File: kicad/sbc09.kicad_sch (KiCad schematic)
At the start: 77 parts, among them J1 Conn_01x03_Male, J2 Conn_01x06_Male, J3 Conn_01x06_Male, J4 Conn_01x06_Male, J5 DB9_Female_MountingHoles, J6 Conn_02x25_Odd_Even, Q1 2N7000, SW1 SW_Push, U1 74LS245, U10 74LS670, U11 74LS670, U12 AS6C4008-55PCN, U13 SST39SF040-DIP, U14 SST39SF040-DIP, U15 XR68C681CJ, U16 MAX232, U2 74LS245, U3 74LS245, U4 MC6809E, U5 74HCT125, U6 ATF22V10C, U7 ATF22V10C, U8 74LS670, U9 74LS670, X1 8MHz, X2 3.6864MHz

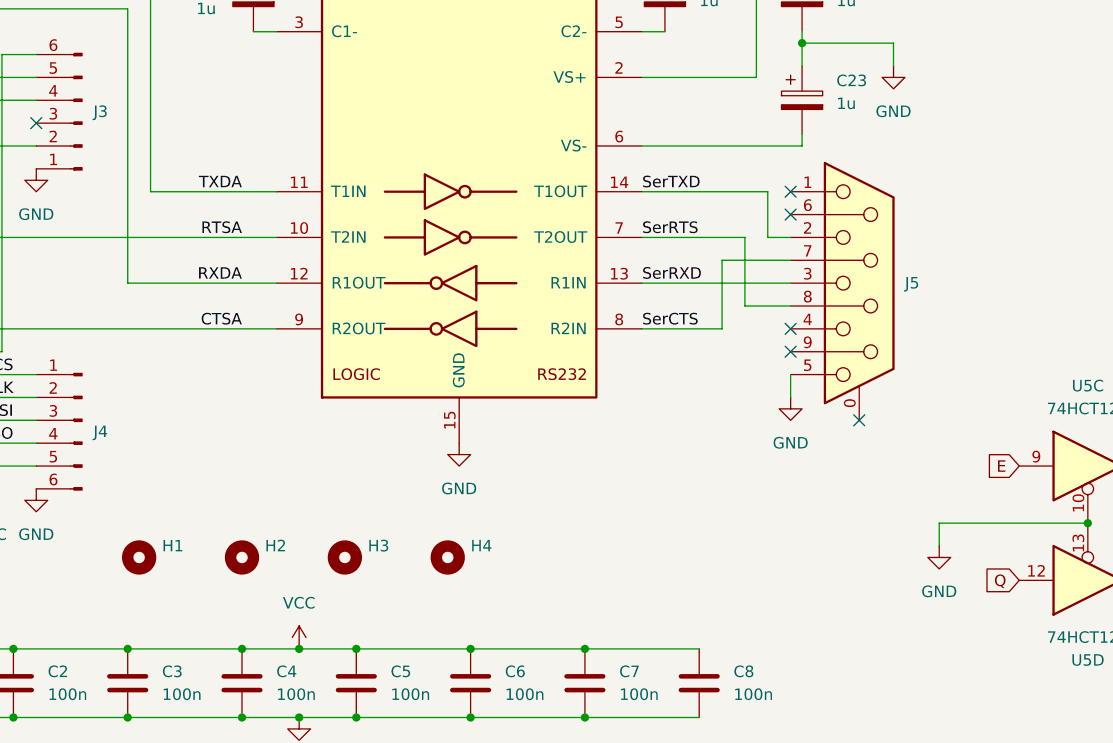
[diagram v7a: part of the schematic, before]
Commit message: Replaced 9-pin D-Sub with 10-pin header
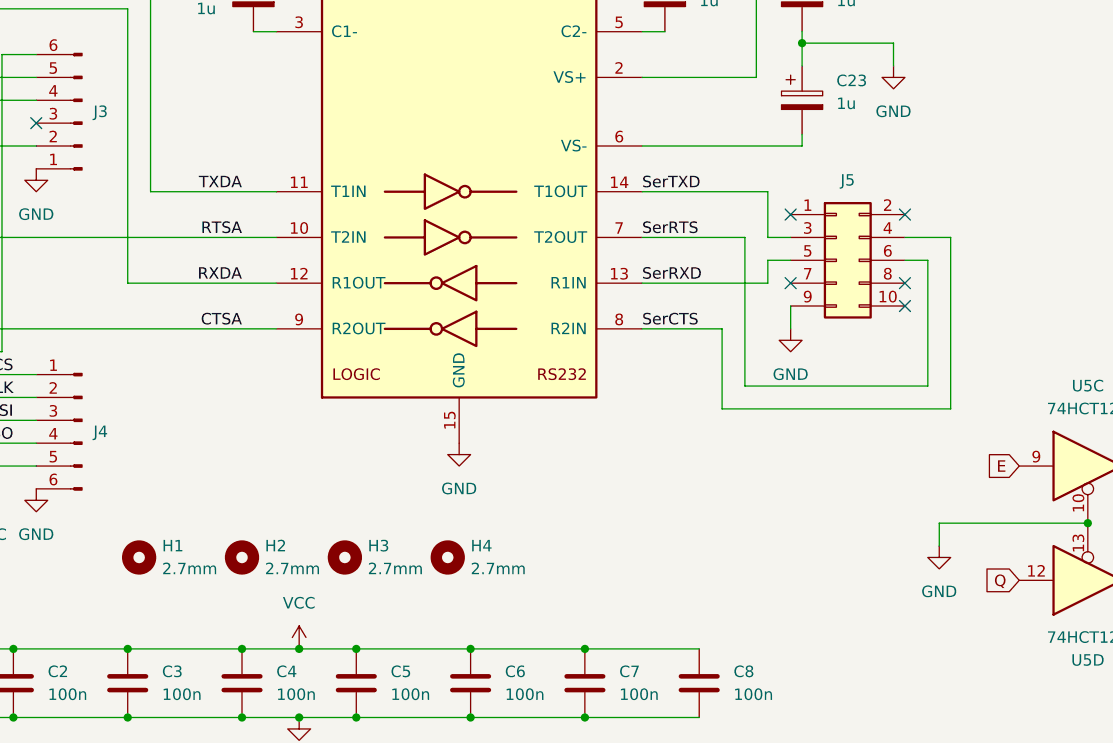
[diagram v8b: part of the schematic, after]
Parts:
- removed J5: DB9_Female_MountingHoles, Connector_Dsub:DSUB-9_Female_Horizontal_P2.77x2.84mm_EdgePinOffset7.70mm_Housed_MountingHolesOffset9.12mm, symbol Connector:DB9_Female_MountingHoles
- added J5: (no value), symbol Connector_Generic:Conn_02x05_Odd_Even
- D1: footprint LED_THT:LED_D3.0mm_Horizontal_O6.35mm_Z2.0mm -> (none)
- H1, H2, H3, H4: value (none) -> 2.7mm
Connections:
- net GND: now also J5.9 (Pin_9)
- net SerCTS: now also J5.4 (Pin_4)
- net SerRTS: now also J5.6 (Pin_6)
- net SerRXD: now also J5.5 (Pin_5)
- net SerTXD: now also J5.3 (Pin_3)
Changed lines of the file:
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@@
   (no_connect (at 16.51 185.42))
   (no_connect (at 377.19 199.39))
+  (no_connect (at 313.69 210.82))
   (no_connect (at 217.17 190.5))
   (no_connect (at 389.89 212.09))
-  (no_connect (at 300.99 198.12))
   (no_connect (at 300.99 200.66))
-  (no_connect (at 300.99 213.36))
-  (no_connect (at 300.99 215.9))
-  (no_connect (at 308.61 223.52))
+  (no_connect (at 300.99 208.28))
+  (no_connect (at 313.69 200.66))
+  (no_connect (at 313.69 208.28))
   (bus_entry (at 199.39 48.26) (size 2.54 2.54)
     (stroke (width 0) (type default) (color 0 0 0 0))
@@
     (stroke (width 0) (type default) (color 0 0 0 0))
   )
+  (wire (pts (xy 313.69 203.2) (xy 318.77 203.2))
+    (stroke (width 0) (type default) (color 0 0 0 0))
+  )
   (wire (pts (xy 284.48 172.72) (xy 287.02 172.72))
     (stroke (width 0) (type default) (color 0 0 0 0))
@@
     (stroke (width 0) (type default) (color 0 0 0 0))
   )
+  (wire (pts (xy 318.77 222.25) (xy 293.37 222.25))
+    (stroke (width 0) (type default) (color 0 0 0 0))
+  )
   (bus (pts (xy 400.05 186.69) (xy 400.05 189.23))
     (stroke (width 0) (type default) (color 0 0 0 0))
@@
     (stroke (width 0) (type default) (color 0 0 0 0))
   )
+  (wire (pts (xy 293.37 222.25) (xy 293.37 213.36))
+    (stroke (width 0) (type default) (color 0 0 0 0))
+  )
   (bus (pts (xy 322.58 142.24) (xy 322.58 128.27))
     (stroke (width 0) (type default) (color 0 0 0 0))
@@
     (stroke (width 0) (type default) (color 0 0 0 0))
   )
+  (wire (pts (xy 318.77 203.2) (xy 318.77 222.25))
+    (stroke (width 0) (type default) (color 0 0 0 0))
+  )
   (wire (pts (xy 227.33 177.8) (xy 227.33 208.28))
     (stroke (width 0) (type default) (color 0 0 0 0))
@@
     (stroke (width 0) (type default) (color 0 0 0 0))
   )
+  (wire (pts (xy 298.45 208.28) (xy 298.45 205.74))
+    (stroke (width 0) (type default) (color 0 0 0 0))
+  )
   (bus (pts (xy 91.44 123.19) (xy 91.44 135.89))
     (stroke (width 0) (type default) (color 0 0 0 0))
@@
     (stroke (width 0) (type default) (color 0 0 0 0))
   )
-  (wire (pts (xy 300.99 205.74) (xy 293.37 205.74))
-    (stroke (width 0) (type default) (color 0 0 0 0))
-  )
   (bus (pts (xy 245.11 142.24) (xy 201.93 142.24))
     (stroke (width 0) (type default) (color 0 0 0 0))
@@
     (stroke (width 0) (type default) (color 0 0 0 0))
   )
+  (wire (pts (xy 298.45 205.74) (xy 300.99 205.74))
+    (stroke (width 0) (type default) (color 0 0 0 0))
+  )
   (wire (pts (xy 256.54 111.76) (xy 259.08 111.76))
     (stroke (width 0) (type default) (color 0 0 0 0))
@@
     (stroke (width 0) (type default) (color 0 0 0 0))
   )
+  (wire (pts (xy 316.23 205.74) (xy 313.69 205.74))
+    (stroke (width 0) (type default) (color 0 0 0 0))
+  )
   (bus (pts (xy 96.52 195.58) (xy 96.52 198.12))
     (stroke (width 0) (type default) (color 0 0 0 0))
@@
     (stroke (width 0) (type default) (color 0 0 0 0))
   )
+  (wire (pts (xy 316.23 219.71) (xy 316.23 205.74))
+    (stroke (width 0) (type default) (color 0 0 0 0))
+  )
   (bus (pts (xy 304.8 63.5) (xy 304.8 66.04))
     (stroke (width 0) (type default) (color 0 0 0 0))
@@
     (stroke (width 0) (type default) (color 0 0 0 0))
   )
-  (wire (pts (xy 293.37 205.74) (xy 293.37 213.36))
-    (stroke (width 0) (type default) (color 0 0 0 0))
-  )
   (bus (pts (xy 297.18 53.34) (xy 297.18 50.8))
     (stroke (width 0) (type default) (color 0 0 0 0))
@@
     (stroke (width 0) (type default) (color 0 0 0 0))
   )
-  (wire (pts (xy 300.99 210.82) (xy 295.91 210.82))
-    (stroke (width 0) (type default) (color 0 0 0 0))
-  )
   (wire (pts (xy 210.82 40.64) (xy 215.9 40.64))
     (stroke (width 0) (type default) (color 0 0 0 0))
   )
-  (wire (pts (xy 300.99 203.2) (xy 298.45 203.2))
+  (wire (pts (xy 298.45 203.2) (xy 300.99 203.2))
     (stroke (width 0) (type default) (color 0 0 0 0))
   )
@@
     (stroke (width 0) (type default) (color 0 0 0 0))
   )
-  (wire (pts (xy 300.99 218.44) (xy 300.99 220.98))
+  (wire (pts (xy 300.99 210.82) (xy 300.99 213.36))
     (stroke (width 0) (type default) (color 0 0 0 0))
   )
@@
     (stroke (width 0) (type default) (color 0 0 0 0))
   )
-  (wire (pts (xy 284.48 208.28) (xy 300.99 208.28))
+  (wire (pts (xy 284.48 208.28) (xy 298.45 208.28))
     (stroke (width 0) (type default) (color 0 0 0 0))
   )
@@
     (stroke (width 0) (type default) (color 0 0 0 0))
   )
-  (wire (pts (xy 295.91 210.82) (xy 295.91 203.2))
+  (wire (pts (xy 295.91 203.2) (xy 295.91 219.71))
     (stroke (width 0) (type default) (color 0 0 0 0))
   )
@@
     (stroke (width 0) (type default) (color 0 0 0 0))
   )
+  (wire (pts (xy 295.91 219.71) (xy 316.23 219.71))
+    (stroke (width 0) (type default) (color 0 0 0 0))
+  )
   (wire (pts (xy 67.31 175.26) (xy 87.63 175.26))
     (stroke (width 0) (type default) (color 0 0 0 0))
@@
       (effects (font (size 1.27 1.27)) (justify left))
     )
-    (property "Value" "" (id 1) (at 231.14 240.0299 0)
+    (property "Value" "2.7mm" (id 1) (at 231.14 240.0299 0)
       (effects (font (size 1.27 1.27)) (justify left))
     )
@@
       (effects (font (size 1.27 1.27)) (justify left))
     )
-    (property "Value" "" (id 1) (at 242.57 240.0299 0)
+    (property "Value" "2.7mm" (id 1) (at 242.57 240.0299 0)
       (effects (font (size 1.27 1.27)) (justify left))
     )
@@
       (effects (font (size 1.27 1.27)) (justify left))
     )
-    (property "Value" "" (id 1) (at 254 240.0299 0)
+    (property "Value" "2.7mm" (id 1) (at 254 240.0299 0)
       (effects (font (size 1.27 1.27)) (justify left))
     )
@@
     (pin "1")
   )
-  (symbol (lib_id "Connector:DB9_Female_MountingHoles") (at 308.61 208.28 0) (unit 1)
-    (in_bom yes) (on_board yes) (fields_autoplaced)
-    (property "Reference" "J5" (id 0) (at 313.69 208.2799 0)
-      (effects (font (size 1.27 1.27)) (justify left))
-    )
-    (property "Value" "DB9_Female_MountingHoles" (id 1) (at 313.69 209.5499 0)
-      (effects (font (size 1.27 1.27)) (justify left) hide)
-    )
-    (property "Footprint" "Connector_Dsub:DSUB-9_Female_Horizontal_P2.77x2.84mm_EdgePinOffset7.70mm_Housed_MountingHolesOffset9.12mm" (id 2) (at 308.61 208.28 0)
-      (effects (font (size 1.27 1.27)) hide)
-    )
-    (property "Datasheet" " ~" (id 3) (at 308.61 208.28 0)
-      (effects (font (size 1.27 1.27)) hide)
-    )
-    (pin "0")
-    (pin "1")
-    (pin "2")
-    (pin "3")
-    (pin "4")
-    (pin "5")
-    (pin "6")
-    (pin "7")
-    (pin "8")
-    (pin "9")
-  )
   (symbol (lib_id "Logic_Programmable:PAL24") (at 62.23 205.74 0) (unit 1)
     (in_bom yes) (on_board yes)
@@
       (effects (font (size 1.27 1.27)) (justify left))
     )
-    (property "Value" "" (id 1) (at 265.43 240.0299 0)
+    (property "Value" "2.7mm" (id 1) (at 265.43 240.0299 0)
       (effects (font (size 1.27 1.27)) (justify left))
     )
@@
     (pin "1")
   )
-  (symbol (lib_id "power:GND") (at 300.99 220.98 0) (unit 1)
+  (symbol (lib_id "power:GND") (at 300.99 213.36 0) (unit 1)
     (in_bom yes) (on_board yes) (fields_autoplaced)
-    (property "Reference" "#PWR054" (id 0) (at 300.99 227.33 0)
+    (property "Reference" "#PWR054" (id 0) (at 300.99 219.71 0)
       (effects (font (size 1.27 1.27)) hide)
     )
-    (property "Value" "GND" (id 1) (at 300.99 226.06 0))
-    (property "Footprint" "" (id 2) (at 300.99 220.98 0)
+    (property "Value" "GND" (id 1) (at 300.99 218.44 0))
+    (property "Footprint" "" (id 2) (at 300.99 213.36 0)
       (effects (font (size 1.27 1.27)) hide)
     )
-    (property "Datasheet" "" (id 3) (at 300.99 220.98 0)
+    (property "Datasheet" "" (id 3) (at 300.99 213.36 0)
       (effects (font (size 1.27 1.27)) hide)
     )
@@
     (pin "9")
   )
+  (symbol (lib_id "Connector_Generic:Conn_02x05_Odd_Even") (at 306.07 205.74 0) (unit 1)
+    (in_bom yes) (on_board yes) (fields_autoplaced)
+    (property "Reference" "J5" (id 0) (at 307.34 196.85 0))
+    (property "Value" "" (id 1) (at 307.34 196.85 0)
+      (effects (font (size 1.27 1.27)) hide)
+    )
+    (property "Footprint" "" (id 2) (at 306.07 205.74 0)
+      (effects (font (size 1.27 1.27)) hide)
+    )
+    (property "Datasheet" "~" (id 3) (at 306.07 205.74 0)
+      (effects (font (size 1.27 1.27)) hide)
+    )
+    (pin "1")
+    (pin "10")
+    (pin "2")
+    (pin "3")
+    (pin "4")
+    (pin "5")
+    (pin "6")
+    (pin "7")
+    (pin "8")
+    (pin "9")
+  )
   (symbol (lib_id "Jumper:Jumper_3_Bridged12") (at 252.73 95.25 90) (mirror x) (unit 1)
     (in_bom yes) (on_board yes)
@@
       (effects (font (size 1.27 1.27)) (justify right))
     )
-    (property "Footprint" "LED_THT:LED_D3.0mm_Horizontal_O6.35mm_Z2.0mm" (id 2) (at 190.5 160.02 0)
+    (property "Footprint" "" (id 2) (at 190.5 160.02 0)
       (effects (font (size 1.27 1.27)) hide)
     )
@@
     )
     (path "/fae83aca-d871-4dad-8dca-794c894d9124"
-      (reference "D1") (unit 1) (value "LED") (footprint "LED_THT:LED_D3.0mm_Horizontal_O6.35mm_Z2.0mm")
+      (reference "D1") (unit 1) (value "LED") (footprint "LED_THT:LED_D3.0mm_Horizontal_O1.27mm_Z2.0mm")
     )
     (path "/0fdc7ebb-4b15-4947-a92f-73b17a1787e1"
@@
       (reference "J4") (unit 1) (value "Conn_01x06_Male") (footprint "Connector_PinSocket_2.54mm:PinSocket_1x06_P2.54mm_Horizontal")
     )
-    (path "/716fe987-5728-4e91-8766-9b4b10dd1846"
-      (reference "J5") (unit 1) (value "DB9_Female_MountingHoles") (footprint "Connector_Dsub:DSUB-9_Female_Horizontal_P2.77x2.84mm_EdgePinOffset7.70mm_Housed_MountingHolesOffset9.12mm")
+    (path "/ea3b1f56-76ac-49a6-b527-33d801875fe4"
+      (reference "J5") (unit 1) (value "Conn_02x05_Odd_Even") (footprint "Connector_PinHeader_2.54mm:PinHeader_2x05_P2.54mm_Vertical")
     )
     (path "/4334d44f-de7d-4517-a909-c9112eb26575"
